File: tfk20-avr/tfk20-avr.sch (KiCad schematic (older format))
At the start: 30 parts, among them J1 USB_C_Receptacle_USB2.0, J2 AVR-ISP-6, SW1 Reset, U1 ATmega32U4-AU, Y1 16MHz

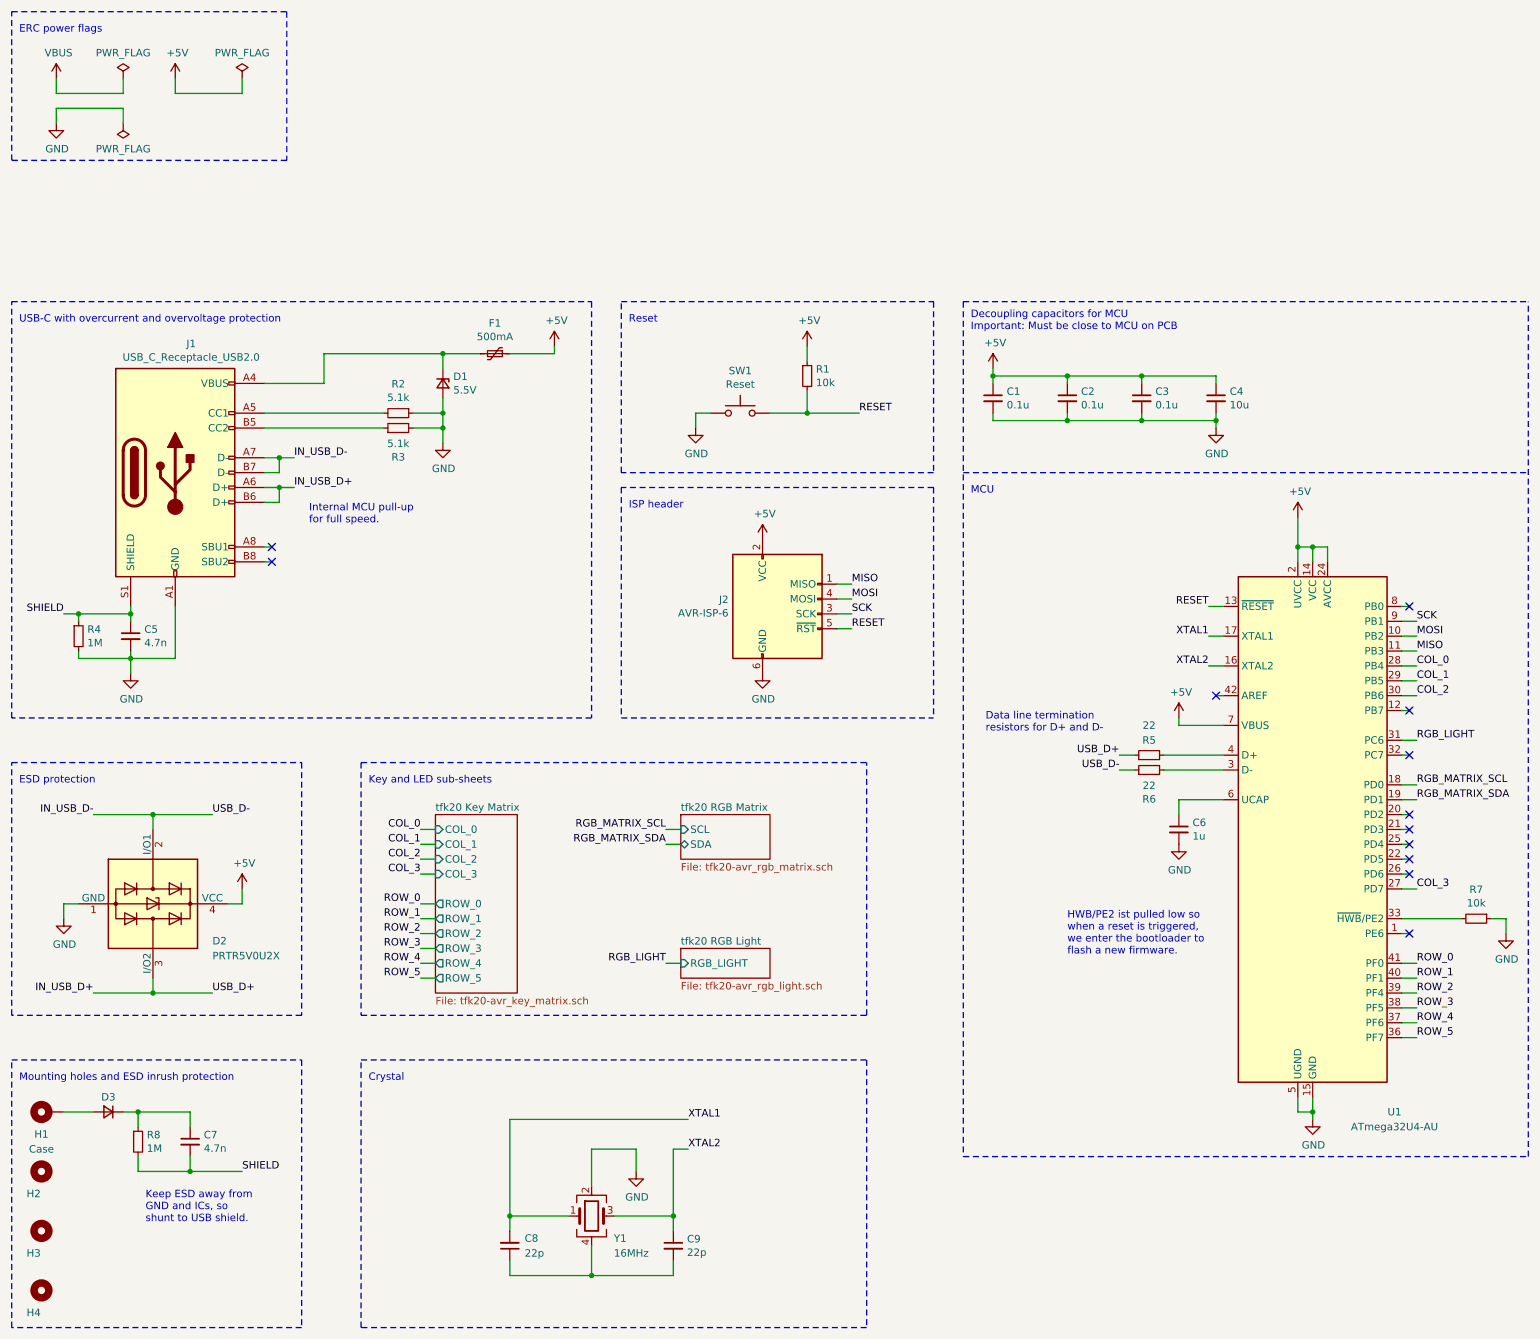
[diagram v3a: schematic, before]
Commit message: Assign some footprints
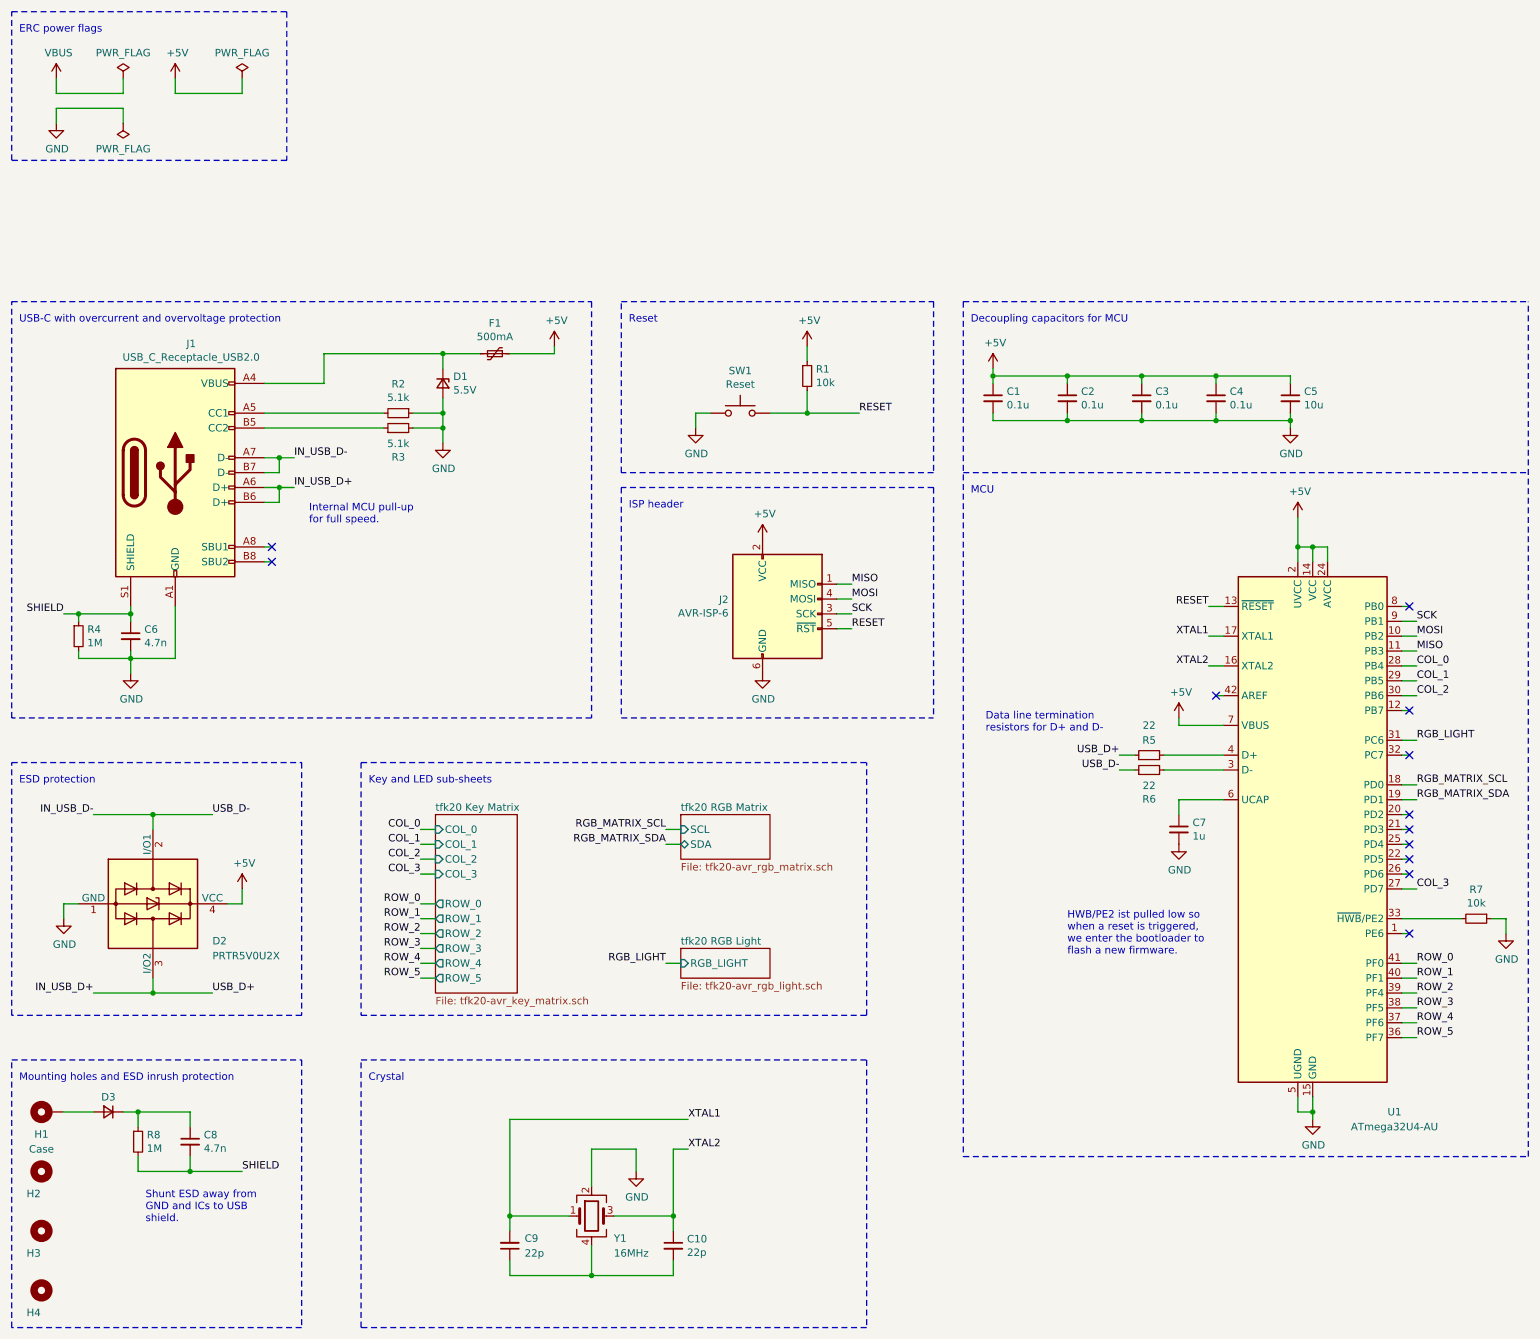
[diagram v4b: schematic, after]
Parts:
- added C4: 0.1u, Capacitor_SMD:C_0805_2012Metric_Pad1.18x1.45mm_HandSolder, symbol Device:C_Small
- C1, C2, C3: footprint (none) -> Capacitor_SMD:C_0805_2012Metric_Pad1.18x1.45mm_HandSolder
- C10: renamed from C9; footprint (none) -> Capacitor_SMD:C_0805_2012Metric_Pad1.18x1.45mm_HandSolder
- C5: renamed from C4; footprint (none) -> Capacitor_SMD:C_0805_2012Metric_Pad1.18x1.45mm_HandSolder
- C6: renamed from C5; footprint (none) -> Capacitor_SMD:C_0805_2012Metric_Pad1.18x1.45mm_HandSolder
- C7: renamed from C6; footprint (none) -> Capacitor_SMD:C_0805_2012Metric_Pad1.18x1.45mm_HandSolder
- C8: renamed from C7; footprint (none) -> Capacitor_SMD:C_0805_2012Metric_Pad1.18x1.45mm_HandSolder
- C9: renamed from C8; footprint (none) -> Capacitor_SMD:C_0805_2012Metric_Pad1.18x1.45mm_HandSolder
- D1: footprint (none) -> Diode_SMD:D_SOD-123
- D3: value D_Small -> Case ESD; footprint (none) -> Diode_SMD:D_SOD-123
- F1: footprint (none) -> Fuse:Fuse_1206_3216Metric_Pad1.42x1.75mm_HandSolder
- R1, R2, R3, R4, R5, R6, R7, R8: footprint (none) -> Resistor_SMD:R_0815_2038Metric_Pad1.20x4.05mm_HandSolder
- Y1: footprint (none) -> Crystal:Crystal_SMD_3225-4Pin_3.2x2.5mm_HandSoldering
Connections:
- net +5V: now also C4.1
- net GND: now also C4.2
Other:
- note added: "Decoupling capacitors for MCU"
- note added: "Shunt ESD away from \nGND and ICs to USB \nshield."
- note removed: "Decoupling capacitors for MCU\nImportant: Must be close to MCU on PCB"
- note removed: "Keep ESD away from \nGND and ICs, so \nshunt to USB shield."
- moved on the sheet: C5
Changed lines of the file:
@@
 COL_3
 $Comp
-L Device:C_Small C5
+L Device:C_Small C6
 U 1 1 6026C0EC
 P 1500 2950
-F 0 "C5" H 1592 2996 50  0000 L CNN
+F 0 "C6" H 1592 2996 50  0000 L CNN
 F 1 "4.7n" H 1592 2905 50  0000 L CNN
-F 2 "" H 1500 2950 50  0001 C CNN
+F 2 "Capacitor_SMD:C_0805_2012Metric_Pad1.18x1.45mm_HandSolder" H 1500 2950 50  0001 C CNN
 F 3 "~" H 1500 2950 50  0001 C CNN
 	1    1500 2950
@@
 F 0 "R4" H 1209 2996 50  0000 L CNN
 F 1 "1M" H 1209 2905 50  0000 L CNN
-F 2 "" H 1150 2950 50  0001 C CNN
+F 2 "Resistor_SMD:R_0815_2038Metric_Pad1.20x4.05mm_HandSolder" H 1150 2950 50  0001 C CNN
 F 3 "~" H 1150 2950 50  0001 C CNN
 	1    1150 2950
@@
 Text Notes 2700 2200 0    50   ~ 0
 Internal MCU pull-up \nfor full speed.
-Text Notes 7150 900  0    50   ~ 0
-Decoupling capacitors for MCU\nImportant: Must be close to MCU on PCB
+Text Notes 7150 850  0    50   ~ 0
+Decoupling capacitors for MCU
 $Sheet
 S 5200 4150 600  300
@@
 AR Path="/60815FFC/60989164" Ref="D?"  Part="1"
 F 0 "D3" H 1350 6050 50  0000 C CNN
-F 1 "D_Small" H 1350 6034 50  0001 C CNN
-F 2 "" V 1350 6150 50  0001 C CNN
+F 1 "Case ESD" H 1350 6034 50  0001 C CNN
+F 2 "Diode_SMD:D_SOD-123" V 1350 6150 50  0001 C CNN
 F 3 "~" V 1350 6150 50  0001 C CNN
 	1    1350 6150
@@
 F 0 "R8" H 1609 6396 50  0000 L CNN
 F 1 "1M" H 1609 6305 50  0000 L CNN
-F 2 "" H 1550 6350 50  0001 C CNN
+F 2 "Resistor_SMD:R_0815_2038Metric_Pad1.20x4.05mm_HandSolder" H 1550 6350 50  0001 C CNN
 F 3 "~" H 1550 6350 50  0001 C CNN
 	1    1550 6350
@@
 $EndComp
 $Comp
-L Device:C_Small C7
+L Device:C_Small C8
 U 1 1 60989175
 P 1900 6350
-AR Path="/60989175" Ref="C7"  Part="1"
+AR Path="/60989175" Ref="C8"  Part="1"
 AR Path="/60815FFC/60989175" Ref="C?"  Part="1"
-F 0 "C7" H 1992 6396 50  0000 L CNN
+F 0 "C8" H 1992 6396 50  0000 L CNN
 F 1 "4.7n" H 1992 6305 50  0000 L CNN
-F 2 "" H 1900 6350 50  0001 C CNN
+F 2 "Capacitor_SMD:C_0805_2012Metric_Pad1.18x1.45mm_HandSolder" H 1900 6350 50  0001 C CNN
 F 3 "~" H 1900 6350 50  0001 C CNN
 	1    1900 6350
@@
 SHIELD
 Text Notes 1600 6900 0    50   ~ 0
-Keep ESD away from \nGND and ICs, so \nshunt to USB shield.
+Shunt ESD away from \nGND and ICs to USB \nshield.
 Wire Wire Line
 	4350 1050 4350 1000
@@
 F 0 "F1" V 3745 1050 50  0000 C CNN
 F 1 "500mA" V 3836 1050 50  0000 C CNN
-F 2 "" H 4000 850 50  0001 L CNN
+F 2 "Fuse:Fuse_1206_3216Metric_Pad1.42x1.75mm_HandSolder" H 4000 850 50  0001 L CNN
 F 3 "~" H 3950 1050 50  0001 C CNN
 	1    3950 1050
@@
 F 0 "R6" V 8154 3850 50  0000 C CNN
 F 1 "22" V 8245 3850 50  0000 C CNN
-F 2 "" H 8350 3850 50  0001 C CNN
+F 2 "Resistor_SMD:R_0815_2038Metric_Pad1.20x4.05mm_HandSolder" H 8350 3850 50  0001 C CNN
 F 3 "~" H 8350 3850 50  0001 C CNN
 	1    8350 3850
@@
 F 0 "R5" V 8450 3750 50  0000 C CNN
 F 1 "22" V 8550 3750 50  0000 C CNN
-F 2 "" H 8350 3750 50  0001 C CNN
+F 2 "Resistor_SMD:R_0815_2038Metric_Pad1.20x4.05mm_HandSolder" H 8350 3750 50  0001 C CNN
 F 3 "~" H 8350 3750 50  0001 C CNN
 	1    8350 3750
@@
 F 0 "R2" V 3104 1450 50  0000 C CNN
 F 1 "5.1k" V 3195 1450 50  0000 C CNN
-F 2 "" H 3300 1450 50  0001 C CNN
+F 2 "Resistor_SMD:R_0815_2038Metric_Pad1.20x4.05mm_HandSolder" H 3300 1450 50  0001 C CNN
 F 3 "~" H 3300 1450 50  0001 C CNN
 	1    3300 1450
@@
 F 0 "R3" V 3104 1550 50  0000 C CNN
 F 1 "5.1k" V 3195 1550 50  0000 C CNN
-F 2 "" H 3300 1550 50  0001 C CNN
+F 2 "Resistor_SMD:R_0815_2038Metric_Pad1.20x4.05mm_HandSolder" H 3300 1550 50  0001 C CNN
 F 3 "~" H 3300 1550 50  0001 C CNN
 	1    3300 1550
@@
 F 0 "R7" V 10354 4850 50  0000 C CNN
 F 1 "10k" V 10445 4850 50  0000 C CNN
-F 2 "" H 10550 4850 50  0001 C CNN
+F 2 "Resistor_SMD:R_0815_2038Metric_Pad1.20x4.05mm_HandSolder" H 10550 4850 50  0001 C CNN
 F 3 "~" H 10550 4850 50  0001 C CNN
 	1    10550 4850
@@
 $EndComp
 $Comp
-L Device:C_Small C6
+L Device:C_Small C7
 U 1 1 60E2DC6A
 P 8550 4250
-F 0 "C6" H 8642 4296 50  0000 L CNN
+F 0 "C7" H 8642 4296 50  0000 L CNN
 F 1 "1u" H 8642 4205 50  0000 L CNN
-F 2 "" H 8550 4250 50  0001 C CNN
+F 2 "Capacitor_SMD:C_0805_2012Metric_Pad1.18x1.45mm_HandSolder" H 8550 4250 50  0001 C CNN
 F 3 "~" H 8550 4250 50  0001 C CNN
 	1    8550 4250
@@
 F 0 "C1" H 7392 1396 50  0000 L CNN
 F 1 "0.1u" H 7392 1305 50  0000 L CNN
-F 2 "" H 7300 1350 50  0001 C CNN
+F 2 "Capacitor_SMD:C_0805_2012Metric_Pad1.18x1.45mm_HandSolder" H 7300 1350 50  0001 C CNN
 F 3 "~" H 7300 1350 50  0001 C CNN
 	1    7300 1350
@@
 $EndComp
 $Comp
-L Device:C_Small C4
+L Device:C_Small C5
 U 1 1 60E7A085
-P 8800 1350
-F 0 "C4" H 8892 1396 50  0000 L CNN
-F 1 "10u" H 8892 1305 50  0000 L CNN
-F 2 "" H 8800 1350 50  0001 C CNN
-F 3 "~" H 8800 1350 50  0001 C CNN
-	1    8800 1350
+P 9300 1350
+F 0 "C5" H 9392 1396 50  0000 L CNN
+F 1 "10u" H 9392 1305 50  0000 L CNN
+F 2 "Capacitor_SMD:C_0805_2012Metric_Pad1.18x1.45mm_HandSolder" H 9300 1350 50  0001 C CNN
+F 3 "~" H 9300 1350 50  0001 C CNN
+	1    9300 1350
 	1    0    0    -1
 $EndComp
@@
 F 0 "C2" H 7892 1396 50  0000 L CNN
 F 1 "0.1u" H 7892 1305 50  0000 L CNN
-F 2 "" H 7800 1350 50  0001 C CNN
+F 2 "Capacitor_SMD:C_0805_2012Metric_Pad1.18x1.45mm_HandSolder" H 7800 1350 50  0001 C CNN
 F 3 "~" H 7800 1350 50  0001 C CNN
 	1    7800 1350
@@
 F 0 "C3" H 8392 1396 50  0000 L CNN
 F 1 "0.1u" H 8392 1305 50  0000 L CNN
-F 2 "" H 8300 1350 50  0001 C CNN
+F 2 "Capacitor_SMD:C_0805_2012Metric_Pad1.18x1.45mm_HandSolder" H 8300 1350 50  0001 C CNN
 F 3 "~" H 8300 1350 50  0001 C CNN
 	1    8300 1350
@@
 F 0 "R1" H 6109 1246 50  0000 L CNN
 F 1 "10k" H 6109 1155 50  0000 L CNN
-F 2 "" H 6050 1200 50  0001 C CNN
+F 2 "Resistor_SMD:R_0815_2038Metric_Pad1.20x4.05mm_HandSolder" H 6050 1200 50  0001 C CNN
 F 3 "~" H 6050 1200 50  0001 C CNN
 	1    6050 1200
@@
 	7800 1500 8300 1500
 Wire Wire Line
-	8300 1200 8800 1200
-Wire Wire Line
-	8800 1200 8800 1250
-Connection ~ 8300 1200
-Wire Wire Line
-	8800 1450 8800 1500
-Wire Wire Line
-	8800 1500 8300 1500
-Connection ~ 8300 1500
-Wire Wire Line
-	8800 1500 8800 1550
-Connection ~ 8800 1500
+	8800 1200 9300 1200
+Wire Wire Line
+	9300 1200 9300 1250
+Wire Wire Line
+	9300 1450 9300 1500
+Wire Wire Line
+	9300 1500 8800 1500
+Wire Wire Line
+	9300 1500 9300 1550
+Connection ~ 9300 1500
 $Comp
 L power:GND #PWR08
 U 1 1 61059BD9
-P 8800 1550
+P 9300 1550
 AR Path="/61059BD9" Ref="#PWR08"  Part="1"
 AR Path="/60815FFC/61059BD9" Ref="#PWR?"  Part="1"
-F 0 "#PWR08" H 8800 1300 50  0001 C CNN
-F 1 "GND" H 8805 1377 50  0000 C CNN
-F 2 "" H 8800 1550 50  0001 C CNN
-F 3 "" H 8800 1550 50  0001 C CNN
-	1    8800 1550
+F 0 "#PWR08" H 9300 1300 50  0001 C CNN
+F 1 "GND" H 9305 1377 50  0000 C CNN
+F 2 "" H 9300 1550 50  0001 C CNN
+F 3 "" H 9300 1550 50  0001 C CNN
+	1    9300 1550
 	1    0    0    -1
 $EndComp
@@
 F 0 "Y1" H 4750 6700 50  0000 L CNN
 F 1 "16MHz" H 4750 6600 50  0000 L CNN
-F 2 "" H 4600 6850 50  0001 C CNN
+F 2 "Crystal:Crystal_SMD_3225-4Pin_3.2x2.5mm_HandSoldering" H 4600 6850 50  0001 C CNN
 F 3 "~" H 4600 6850 50  0001 C CNN
 	1    4600 6850
@@
 	4600 7050 4600 7250
 $Comp
-L Device:C_Small C9
+L Device:C_Small C10
 U 1 1 611FB100
 P 5150 7050
-F 0 "C9" H 5242 7096 50  0000 L CNN
+F 0 "C10" H 5242 7096 50  0000 L CNN
 F 1 "22p" H 5242 7005 50  0000 L CNN
-F 2 "" H 5150 7050 50  0001 C CNN
+F 2 "Capacitor_SMD:C_0805_2012Metric_Pad1.18x1.45mm_HandSolder" H 5150 7050 50  0001 C CNN
 F 3 "~" H 5150 7050 50  0001 C CNN
 	1    5150 7050
@@
 Connection ~ 4600 7250
 $Comp
-L Device:C_Small C8
+L Device:C_Small C9
 U 1 1 6120D60B
 P 4050 7050
-F 0 "C8" H 3950 7000 50  0000 R CNN
+F 0 "C9" H 3950 7000 50  0000 R CNN
 F 1 "22p" H 3950 7100 50  0000 R CNN
-F 2 "" H 4050 7050 50  0001 C CNN
+F 2 "Capacitor_SMD:C_0805_2012Metric_Pad1.18x1.45mm_HandSolder" H 4050 7050 50  0001 C CNN
 F 3 "~" H 4050 7050 50  0001 C CNN
 	1    4050 7050
@@
 F 0 "D1" V 3554 1320 50  0000 L CNN
 F 1 "5.5V" V 3645 1320 50  0000 L CNN
-F 2 "" V 3600 1250 50  0001 C CNN
+F 2 "Diode_SMD:D_SOD-123" V 3600 1250 50  0001 C CNN
 F 3 "~" V 3600 1250 50  0001 C CNN
 	1    3600 1250
@@
 Text Notes 4850 2100 0    50   ~ 0
 ISP header
+$Comp
+L Device:C_Small C4
+U 1 1 60CE1DC9
+P 8800 1350
+F 0 "C4" H 8892 1396 50  0000 L CNN
+F 1 "0.1u" H 8892 1305 50  0000 L CNN
+F 2 "Capacitor_SMD:C_0805_2012Metric_Pad1.18x1.45mm_HandSolder" H 8800 1350 50  0001 C CNN
+F 3 "~" H 8800 1350 50  0001 C CNN
+	1    8800 1350
+	1    0    0    -1
+$EndComp
+Wire Wire Line
+	8800 1200 8800 1250
+Wire Wire Line
+	8300 1200 8800 1200
+Wire Wire Line
+	8800 1500 8800 1450
+Wire Wire Line
+	8300 1500 8800 1500
+Connection ~ 8300 1200
+Connection ~ 8300 1500
+Connection ~ 8800 1200
+Connection ~ 8800 1500
 $EndSCHEMATC

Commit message: Assigned remaining footprints
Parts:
- H1, H2, H3, H4: footprint (none) -> MountingHole:MountingHole_2.5mm_Pad
- J2: footprint (none) -> random-keyboard-parts:Reset_Pretty-Mask
- SW1: footprint (none) -> random-keyboard-parts:SKQG-1155865
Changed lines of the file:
@@
 F 0 "H1" V 800 6200 50  0000 C CNN
 F 1 "Case" V 700 6200 50  0000 C CNN
-F 2 "" H 950 6150 50  0001 C CNN
+F 2 "MountingHole:MountingHole_2.5mm_Pad" H 950 6150 50  0001 C CNN
 F 3 "~" H 950 6150 50  0001 C CNN
 	1    950  6150
@@
 F 0 "SW1" H 5600 1735 50  0000 C CNN
 F 1 "Reset" H 5600 1644 50  0000 C CNN
-F 2 "" H 5600 1650 50  0001 C CNN
+F 2 "random-keyboard-parts:SKQG-1155865" H 5600 1650 50  0001 C CNN
 F 3 "~" H 5600 1650 50  0001 C CNN
 	1    5600 1450
@@
 F 0 "H2" H 800 6400 50  0000 L CNN
 F 1 "MountingHole" H 1000 6505 50  0001 L CNN
-F 2 "" H 900 6550 50  0001 C CNN
+F 2 "MountingHole:MountingHole_2.5mm_Pad" H 900 6550 50  0001 C CNN
 F 3 "~" H 900 6550 50  0001 C CNN
 	1    900  6550
@@
 F 0 "H3" H 800 6800 50  0000 L CNN
 F 1 "MountingHole" H 1000 6905 50  0001 L CNN
-F 2 "" H 900 6950 50  0001 C CNN
+F 2 "MountingHole:MountingHole_2.5mm_Pad" H 900 6950 50  0001 C CNN
 F 3 "~" H 900 6950 50  0001 C CNN
 	1    900  6950
@@
 F 0 "H4" H 800 7200 50  0000 L CNN
 F 1 "MountingHole" H 1000 7305 50  0001 L CNN
-F 2 "" H 900 7350 50  0001 C CNN
+F 2 "MountingHole:MountingHole_2.5mm_Pad" H 900 7350 50  0001 C CNN
 F 3 "~" H 900 7350 50  0001 C CNN
 	1    900  7350
@@
 F 0 "J2" H 5521 2896 50  0000 R CNN
 F 1 "AVR-ISP-6" H 5521 2805 50  0000 R CNN
-F 2 "" V 5600 2850 50  0001 C CNN
+F 2 "random-keyboard-parts:Reset_Pretty-Mask" V 5600 2850 50  0001 C CNN
 F 3 " ~" H 4575 2250 50  0001 C CNN
 	1    5850 2800

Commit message: Begin PCB
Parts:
- R1, R2, R3, R4, R5, R6, R7, R8: footprint Resistor_SMD:R_0815_2038Metric_Pad1.20x4.05mm_HandSolder -> Resistor_SMD:R_0805_2012Metric_Pad1.20x1.40mm_HandSolder
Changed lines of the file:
@@
 F 0 "R4" H 1209 2996 50  0000 L CNN
 F 1 "1M" H 1209 2905 50  0000 L CNN
-F 2 "Resistor_SMD:R_0815_2038Metric_Pad1.20x4.05mm_HandSolder" H 1150 2950 50  0001 C CNN
+F 2 "Resistor_SMD:R_0805_2012Metric_Pad1.20x1.40mm_HandSolder" H 1150 2950 50  0001 C CNN
 F 3 "~" H 1150 2950 50  0001 C CNN
 	1    1150 2950
@@
 F 0 "R8" H 1609 6396 50  0000 L CNN
 F 1 "1M" H 1609 6305 50  0000 L CNN
-F 2 "Resistor_SMD:R_0815_2038Metric_Pad1.20x4.05mm_HandSolder" H 1550 6350 50  0001 C CNN
+F 2 "Resistor_SMD:R_0805_2012Metric_Pad1.20x1.40mm_HandSolder" H 1550 6350 50  0001 C CNN
 F 3 "~" H 1550 6350 50  0001 C CNN
 	1    1550 6350
@@
 F 0 "R6" V 8154 3850 50  0000 C CNN
 F 1 "22" V 8245 3850 50  0000 C CNN
-F 2 "Resistor_SMD:R_0815_2038Metric_Pad1.20x4.05mm_HandSolder" H 8350 3850 50  0001 C CNN
+F 2 "Resistor_SMD:R_0805_2012Metric_Pad1.20x1.40mm_HandSolder" H 8350 3850 50  0001 C CNN
 F 3 "~" H 8350 3850 50  0001 C CNN
 	1    8350 3850
@@
 F 0 "R5" V 8450 3750 50  0000 C CNN
 F 1 "22" V 8550 3750 50  0000 C CNN
-F 2 "Resistor_SMD:R_0815_2038Metric_Pad1.20x4.05mm_HandSolder" H 8350 3750 50  0001 C CNN
+F 2 "Resistor_SMD:R_0805_2012Metric_Pad1.20x1.40mm_HandSolder" H 8350 3750 50  0001 C CNN
 F 3 "~" H 8350 3750 50  0001 C CNN
 	1    8350 3750
@@
 F 0 "R2" V 3104 1450 50  0000 C CNN
 F 1 "5.1k" V 3195 1450 50  0000 C CNN
-F 2 "Resistor_SMD:R_0815_2038Metric_Pad1.20x4.05mm_HandSolder" H 3300 1450 50  0001 C CNN
+F 2 "Resistor_SMD:R_0805_2012Metric_Pad1.20x1.40mm_HandSolder" H 3300 1450 50  0001 C CNN
 F 3 "~" H 3300 1450 50  0001 C CNN
 	1    3300 1450
@@
 F 0 "R3" V 3104 1550 50  0000 C CNN
 F 1 "5.1k" V 3195 1550 50  0000 C CNN
-F 2 "Resistor_SMD:R_0815_2038Metric_Pad1.20x4.05mm_HandSolder" H 3300 1550 50  0001 C CNN
+F 2 "Resistor_SMD:R_0805_2012Metric_Pad1.20x1.40mm_HandSolder" H 3300 1550 50  0001 C CNN
 F 3 "~" H 3300 1550 50  0001 C CNN
 	1    3300 1550
@@
 F 0 "R7" V 10354 4850 50  0000 C CNN
 F 1 "10k" V 10445 4850 50  0000 C CNN
-F 2 "Resistor_SMD:R_0815_2038Metric_Pad1.20x4.05mm_HandSolder" H 10550 4850 50  0001 C CNN
+F 2 "Resistor_SMD:R_0805_2012Metric_Pad1.20x1.40mm_HandSolder" H 10550 4850 50  0001 C CNN
 F 3 "~" H 10550 4850 50  0001 C CNN
 	1    10550 4850
@@
 F 0 "R1" H 6109 1246 50  0000 L CNN
 F 1 "10k" H 6109 1155 50  0000 L CNN
-F 2 "Resistor_SMD:R_0815_2038Metric_Pad1.20x4.05mm_HandSolder" H 6050 1200 50  0001 C CNN
+F 2 "Resistor_SMD:R_0805_2012Metric_Pad1.20x1.40mm_HandSolder" H 6050 1200 50  0001 C CNN
 F 3 "~" H 6050 1200 50  0001 C CNN
 	1    6050 1200
